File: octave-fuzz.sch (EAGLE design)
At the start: 56 parts, among them T1 2N5089, T2 2N5089, T3 2N5089, T4 2N5089, T5 2N5089

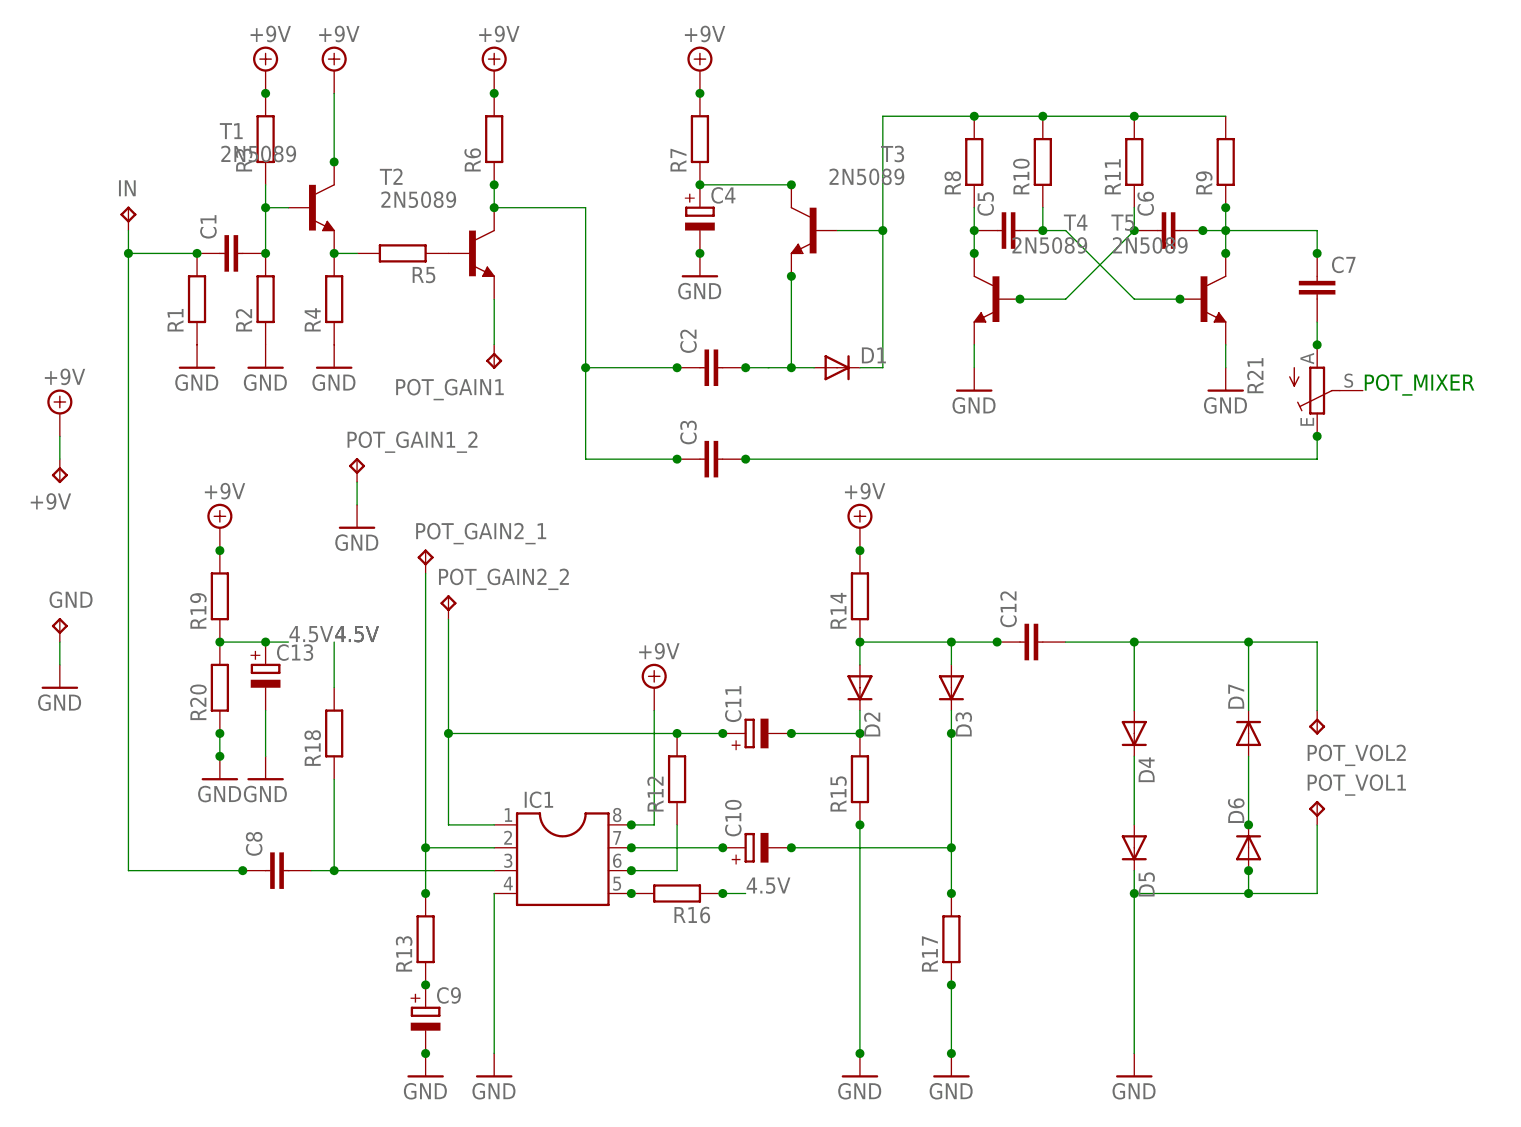
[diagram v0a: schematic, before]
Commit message: added a missing resistor and edited component values
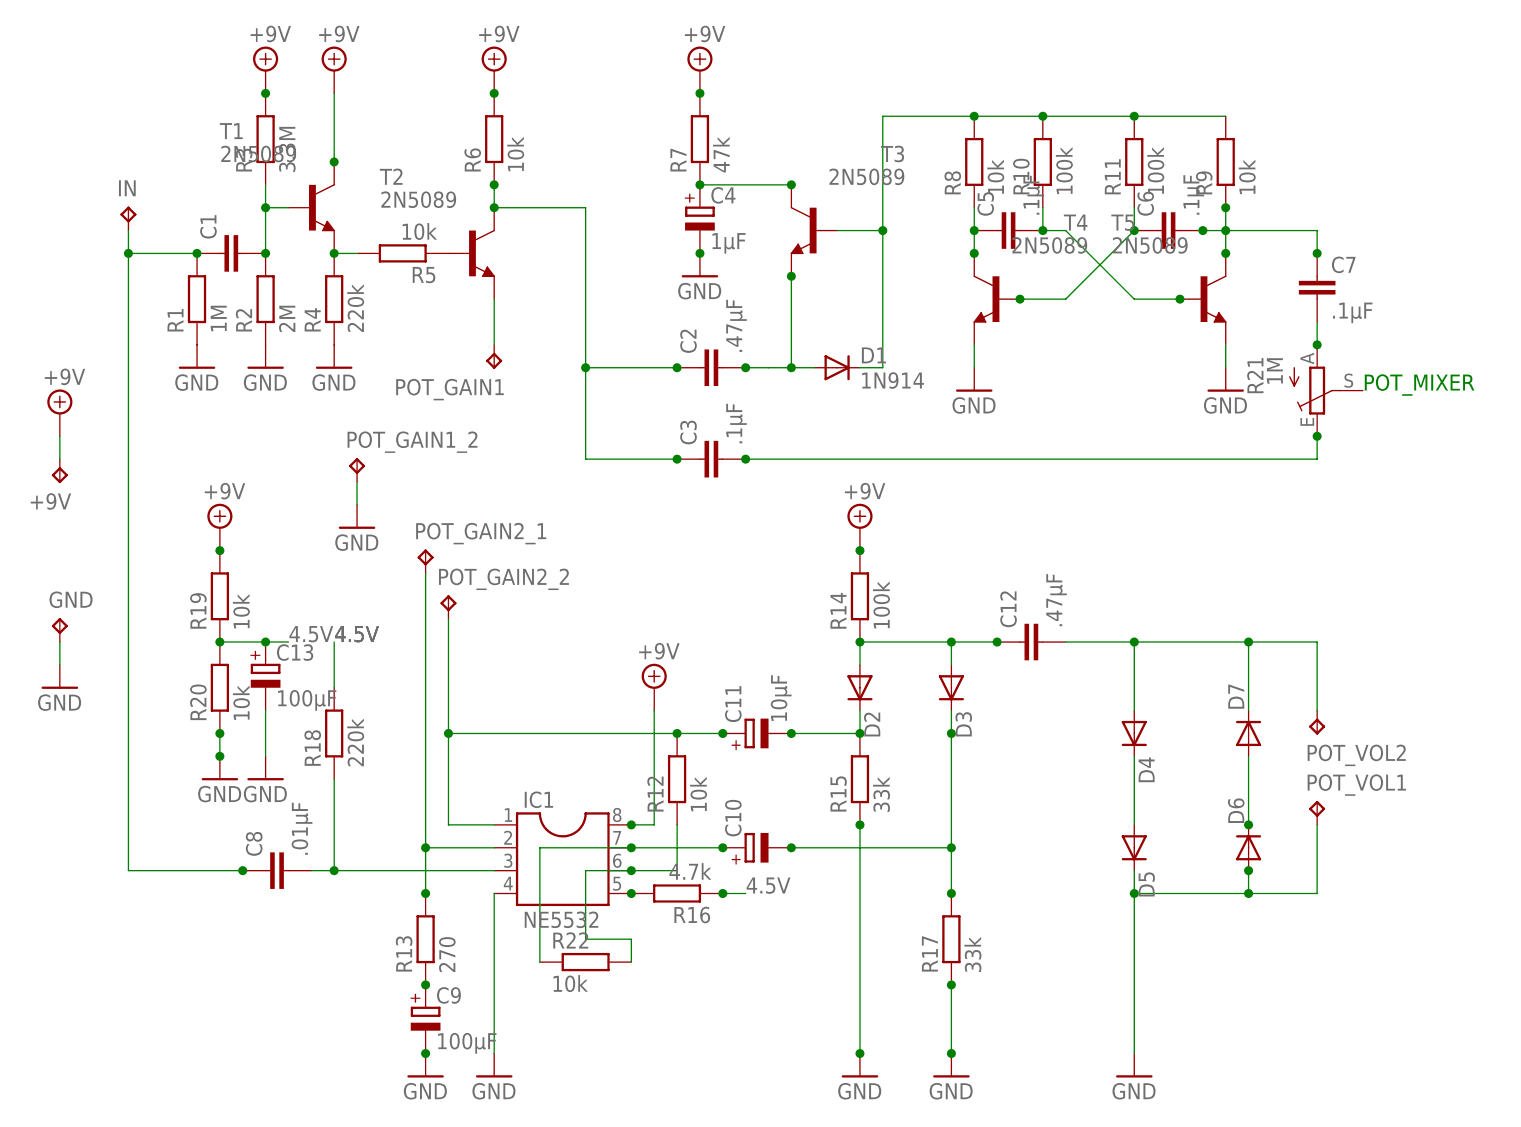
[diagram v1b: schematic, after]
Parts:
- added R22: 10k, resistor:R-EU_0207/10
- C11: value (none) -> 10µF
- C12, C2: value (none) -> .47µF
- C13, C9: value (none) -> 100µF
- C3, C5, C6, C7: value (none) -> .1µF
- C4: value (none) -> 1µF
- C8: value (none) -> .01µF
- D1: value (none) -> 1N914
- IC1: value (none) -> NE5532
- R1, R21: value (none) -> 1M
- R10, R11, R14: value (none) -> 100k
- R12, R19, R20, R5, R6, R8, R9: value (none) -> 10k
- R13: value (none) -> 270
- R15, R17: value (none) -> 33k
- R16: value (none) -> 4.7k
- R18, R4: value (none) -> 220k
- R2: value (none) -> 2M
- R3: value (none) -> 3.3M
- R7: value (none) -> 47k
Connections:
- net N$21: now also R22.2
- net N$22: now also R22.1
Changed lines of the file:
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@@
 <parts>
 <part name="IN" library="testpad" deviceset="TP" device="PAD1-17Y"/>
-<part name="R1" library="resistor" deviceset="R-EU_" device="0207/10"/>
-<part name="R2" library="resistor" deviceset="R-EU_" device="0207/10"/>
-<part name="R3" library="resistor" deviceset="R-EU_" device="0207/10"/>
-<part name="R4" library="resistor" deviceset="R-EU_" device="0207/10"/>
-<part name="R5" library="resistor" deviceset="R-EU_" device="0207/10"/>
-<part name="R6" library="resistor" deviceset="R-EU_" device="0207/10"/>
+<part name="R1" library="resistor" deviceset="R-EU_" device="0207/10" value="1M"/>
+<part name="R2" library="resistor" deviceset="R-EU_" device="0207/10" value="2M"/>
+<part name="R3" library="resistor" deviceset="R-EU_" device="0207/10" value="3.3M"/>
+<part name="R4" library="resistor" deviceset="R-EU_" device="0207/10" value="220k"/>
+<part name="R5" library="resistor" deviceset="R-EU_" device="0207/10" value="10k"/>
+<part name="R6" library="resistor" deviceset="R-EU_" device="0207/10" value="10k"/>
 <part name="GND1" library="supply1" deviceset="GND" device=""/>
 <part name="GND2" library="supply1" deviceset="GND" device=""/>
@@
 <part name="SUPPLY4" library="supply2" deviceset="+9V" device=""/>
 <part name="POT_GAIN1" library="testpad" deviceset="TP" device="PAD1-20Y"/>
-<part name="R7" library="resistor" deviceset="R-EU_" device="0207/10"/>
-<part name="C2" library="rcl" deviceset="C-EU" device="050-025X075"/>
-<part name="C3" library="rcl" deviceset="C-EU" device="050-025X075"/>
-<part name="C4" library="rcl" deviceset="CPOL-EU" device="E3.5-8"/>
+<part name="R7" library="resistor" deviceset="R-EU_" device="0207/10" value="47k"/>
+<part name="C2" library="rcl" deviceset="C-EU" device="050-025X075" value=".47µF"/>
+<part name="C3" library="rcl" deviceset="C-EU" device="050-025X075" value=".1µF"/>
+<part name="C4" library="rcl" deviceset="CPOL-EU" device="E3.5-8" value="1µF"/>
 <part name="GND4" library="supply1" deviceset="GND" device=""/>
 <part name="T3" library="transistor" deviceset="2N5089" device=""/>
-<part name="D1" library="diode" deviceset="DIODE-" device="D-12.5"/>
+<part name="D1" library="diode" deviceset="DIODE-" device="D-12.5" value="1N914"/>
 <part name="T4" library="transistor" deviceset="2N5089" device=""/>
 <part name="T5" library="transistor" deviceset="2N5089" device=""/>
-<part name="R8" library="resistor" deviceset="R-EU_" device="0207/10"/>
-<part name="R9" library="resistor" deviceset="R-EU_" device="0207/10"/>
-<part name="C5" library="rcl" deviceset="C-EU" device="050-025X075"/>
-<part name="C6" library="rcl" deviceset="C-EU" device="050-025X075"/>
-<part name="R10" library="resistor" deviceset="R-EU_" device="0207/10"/>
-<part name="R11" library="resistor" deviceset="R-EU_" device="0207/10"/>
+<part name="R8" library="resistor" deviceset="R-EU_" device="0207/10" value="10k"/>
+<part name="R9" library="resistor" deviceset="R-EU_" device="0207/10" value="10k"/>
+<part name="C5" library="rcl" deviceset="C-EU" device="050-025X075" value=".1µF"/>
+<part name="C6" library="rcl" deviceset="C-EU" device="050-025X075" value=".1µF"/>
+<part name="R10" library="resistor" deviceset="R-EU_" device="0207/10" value="100k"/>
+<part name="R11" library="resistor" deviceset="R-EU_" device="0207/10" value="100k"/>
 <part name="GND5" library="supply1" deviceset="GND" device=""/>
 <part name="GND6" library="supply1" deviceset="GND" device=""/>
-<part name="IC1" library="ic-package" deviceset="DIL8" device=""/>
-<part name="C8" library="rcl" deviceset="C-EU" device="050-025X075"/>
-<part name="R12" library="resistor" deviceset="R-EU_" device="0207/10"/>
-<part name="R13" library="resistor" deviceset="R-EU_" device="0207/10"/>
+<part name="IC1" library="ic-package" deviceset="DIL8" device="" value="NE5532"/>
+<part name="C8" library="rcl" deviceset="C-EU" device="050-025X075" value=".01µF"/>
+<part name="R12" library="resistor" deviceset="R-EU_" device="0207/10" value="10k"/>
+<part name="R13" library="resistor" deviceset="R-EU_" device="0207/10" value="270"/>
 <part name="GND7" library="supply1" deviceset="GND" device=""/>
 <part name="GND8" library="supply1" deviceset="GND" device=""/>
-<part name="C9" library="rcl" deviceset="CPOL-EU" device="E3.5-8"/>
+<part name="C9" library="rcl" deviceset="CPOL-EU" device="E3.5-8" value="100µF"/>
 <part name="SUPPLY5" library="supply2" deviceset="+9V" device=""/>
 <part name="C10" library="rcl" deviceset="CPOL-EU" device="E3.5-8"/>
-<part name="C11" library="rcl" deviceset="CPOL-EU" device="E3.5-8"/>
+<part name="C11" library="rcl" deviceset="CPOL-EU" device="E3.5-8" value="10µF"/>
 <part name="D2" library="diode" deviceset="DIODE-" device="D-12.5"/>
 <part name="D3" library="diode" deviceset="DIODE-" device="D-12.5"/>
@@
 <part name="D6" library="diode" deviceset="DIODE-" device="D-12.5"/>
 <part name="D7" library="diode" deviceset="DIODE-" device="D-12.5"/>
-<part name="R14" library="resistor" deviceset="R-EU_" device="0207/10"/>
+<part name="R14" library="resistor" deviceset="R-EU_" device="0207/10" value="100k"/>
 <part name="SUPPLY6" library="supply2" deviceset="+9V" device=""/>
-<part name="R15" library="resistor" deviceset="R-EU_" device="0207/10"/>
-<part name="R16" library="resistor" deviceset="R-EU_" device="0207/10"/>
+<part name="R15" library="resistor" deviceset="R-EU_" device="0207/10" value="33k"/>
+<part name="R16" library="resistor" deviceset="R-EU_" device="0207/10" value="4.7k"/>
 <part name="GND9" library="supply1" deviceset="GND" device=""/>
 <part name="GND10" library="supply1" deviceset="GND" device=""/>
 <part name="GND11" library="supply1" deviceset="GND" device=""/>
-<part name="C12" library="rcl" deviceset="C-EU" device="050-025X075"/>
-<part name="R17" library="resistor" deviceset="R-EU_" device="0207/10"/>
-<part name="R18" library="resistor" deviceset="R-EU_" device="0207/10"/>
+<part name="C12" library="rcl" deviceset="C-EU" device="050-025X075" value=".47µF"/>
+<part name="R17" library="resistor" deviceset="R-EU_" device="0207/10" value="33k"/>
+<part name="R18" library="resistor" deviceset="R-EU_" device="0207/10" value="220k"/>
 <part name="POT_GAIN2_1" library="testpad" deviceset="TP" device="PAD1-20Y"/>
 <part name="POT_GAIN2_2" library="testpad" deviceset="TP" device="PAD1-20Y"/>
@@
 <part name="SUPPLY7" library="supply2" deviceset="+9V" device=""/>
 <part name="GND13" library="supply1" deviceset="GND" device=""/>
-<part name="R19" library="resistor" deviceset="R-EU_" device="0207/10"/>
-<part name="R20" library="resistor" deviceset="R-EU_" device="0207/10"/>
+<part name="R19" library="resistor" deviceset="R-EU_" device="0207/10" value="10k"/>
+<part name="R20" library="resistor" deviceset="R-EU_" device="0207/10" value="10k"/>
 <part name="GND14" library="supply1" deviceset="GND" device=""/>
-<part name="C13" library="rcl" deviceset="CPOL-EU" device="E3.5-8"/>
-<part name="C7" library="rcl" deviceset="C-EU" device="050-025X075"/>
-<part name="R21" library="pot" deviceset="TRIM_EU-" device="CA9V"/>
+<part name="C13" library="rcl" deviceset="CPOL-EU" device="E3.5-8" value="100µF"/>
+<part name="C7" library="rcl" deviceset="C-EU" device="050-025X075" value=".1µF"/>
+<part name="R21" library="pot" deviceset="TRIM_EU-" device="CA9V" value="1M"/>
 <part name="SUPPLY8" library="supply2" deviceset="+9V" device=""/>
 <part name="GND15" library="supply1" deviceset="GND" device=""/>
 <part name="GND" library="testpad" deviceset="TP" device="PAD1-20Y"/>
 <part name="+9V" library="testpad" deviceset="TP" device="PAD1-20Y"/>
+<part name="R22" library="resistor" deviceset="R-EU_" device="0207/10" value="10k"/>
 </parts>
 <sheets>
@@
 <instance part="GND" gate="G$1" x="10.16" y="20.32"/>
 <instance part="+9V" gate="G$1" x="10.16" y="35.56" rot="R180"/>
+<instance part="R22" gate="G$1" x="68.58" y="-17.78"/>
 </instances>
 <busses>
@@
 <pinref part="R12" gate="G$1" pin="1"/>
 <wire x1="78.74" y1="-7.62" x2="78.74" y2="-2.54" width="0.1524" layer="91"/>
+<pinref part="R22" gate="G$1" pin="2"/>
+<wire x1="73.66" y1="-17.78" x2="73.66" y2="-15.24" width="0.1524" layer="91"/>
+<wire x1="73.66" y1="-15.24" x2="68.58" y2="-15.24" width="0.1524" layer="91"/>
+<wire x1="68.58" y1="-15.24" x2="68.58" y2="-7.62" width="0.1524" layer="91"/>
+<wire x1="68.58" y1="-7.62" x2="73.66" y2="-7.62" width="0.1524" layer="91"/>
 </segment>
 </net>
@@
 <junction x="73.66" y="-5.08"/>
 <junction x="83.82" y="-5.08"/>
-</segment>
-</net>
+<pinref part="R22" gate="G$1" pin="1"/>
+<wire x1="63.5" y1="-17.78" x2="63.5" y2="-5.08" width="0.1524" layer="91"/>
+<wire x1="63.5" y1="-5.08" x2="73.66" y2="-5.08" width="0.1524" layer="91"/>
+</segment>
+</net>
